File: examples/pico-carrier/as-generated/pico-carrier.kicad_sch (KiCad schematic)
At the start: 9 parts, among them J1 5V IN, J3 GP0-GP15, J4 GP16-GP28, PWR, U1 Pico

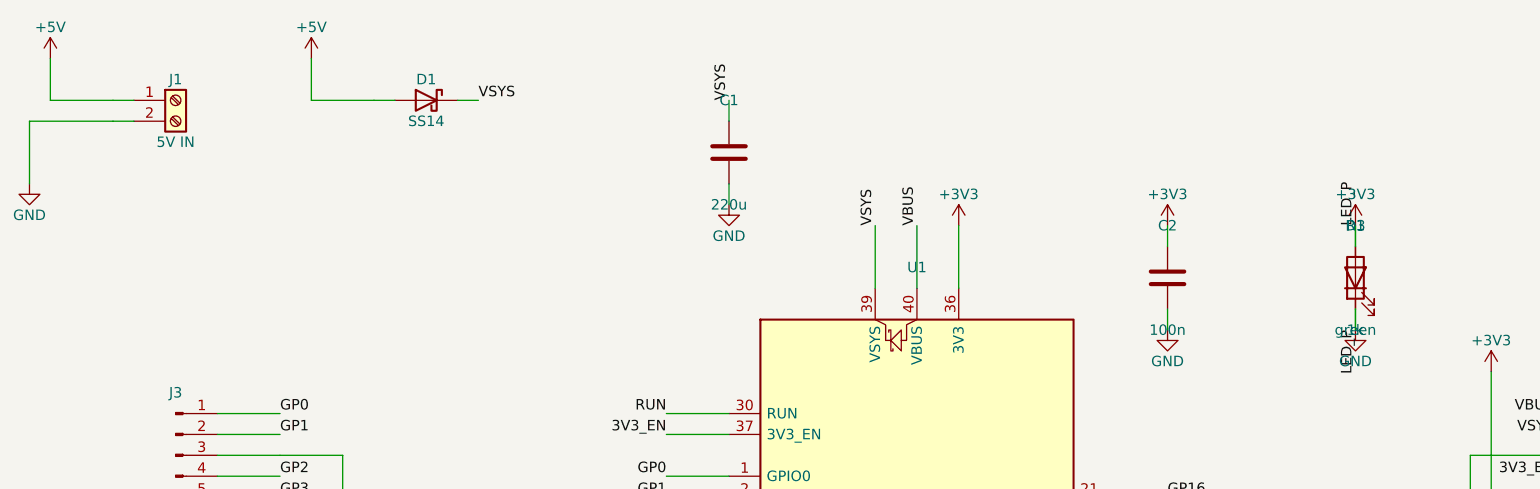
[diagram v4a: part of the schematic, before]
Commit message: Regenerate the four the text and width work changed
Designators and values off the rails they were printed on, power-named
nets at the width their rule asks for, and the buck's feedback ending
on the capacitor pad it senses at.

Co-Authored-By: Claude Fable 5 <noreply@anthropic.com>
Claude-Session: https://claude.ai/code/session_01DUj7Ltu92tWg159mCSacwY
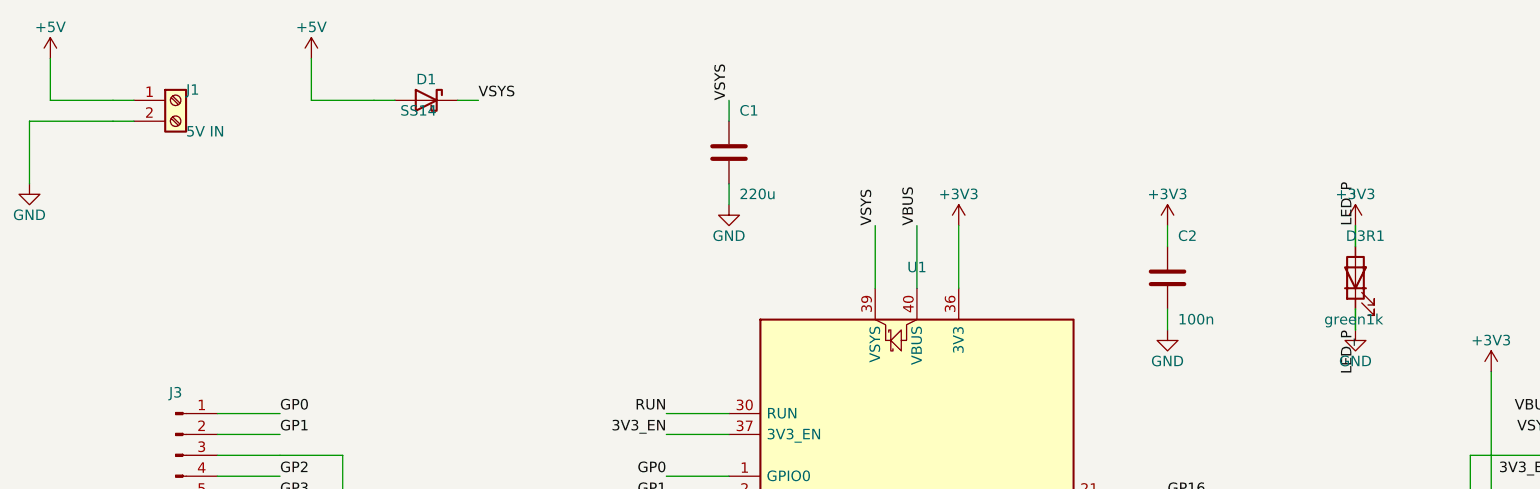
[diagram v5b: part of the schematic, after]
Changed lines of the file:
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@@
   (symbol (lib_id "Connector:Screw_Terminal_01x02") (at 60.0 39.18 0.0) (unit 1)
     (exclude_from_sim no) (in_bom yes) (on_board yes) (dnp no)
-    (property "Reference" "J1" (at 60.0 36.64 0) (effects (font (size 1.27 1.27))))
-    (property "Value" "5V IN" (at 60.0 44.26 0) (effects (font (size 1.27 1.27))))
+    (property "Reference" "J1" (at 61.27 37.91 0) (effects (font (size 1.27 1.27)) (justify left)))
+    (property "Value" "5V IN" (at 61.27 42.99 0) (effects (font (size 1.27 1.27)) (justify left)))
     (property "Footprint" "TerminalBlock_Phoenix:TerminalBlock_Phoenix_MKDS-1,5-2_1x02_P5.00mm_Horizontal" (at 60.0 39.18 0) (effects (font (size 1.27 1.27)) hide))
     (property "Datasheet" "https://www.phoenixcontact.com/product/1729128" (at 60.0 39.18 0) (effects (font (size 1.27 1.27)) hide))
@@
     (exclude_from_sim no) (in_bom yes) (on_board yes) (dnp no)
     (property "Reference" "D1" (at 90.48 36.64 0) (effects (font (size 1.27 1.27))))
-    (property "Value" "SS14" (at 90.48 41.72 0) (effects (font (size 1.27 1.27))))
+    (property "Value" "SS14" (at 91.75 40.45 0) (effects (font (size 1.27 1.27)) (justify left)))
     (property "Footprint" "Diode_SMD:D_SMA" (at 90.48 39.18 0) (effects (font (size 1.27 1.27)) hide))
     (property "Datasheet" "https://www.vishay.com/docs/88746/ss12.pdf" (at 90.48 39.18 0) (effects (font (size 1.27 1.27)) hide))
@@
   (symbol (lib_id "Device:C") (at 127.31 45.53 0.0) (unit 1)
     (exclude_from_sim no) (in_bom yes) (on_board yes) (dnp no)
-    (property "Reference" "C1" (at 127.31 39.18 0) (effects (font (size 1.27 1.27))))
-    (property "Value" "220u" (at 127.31 51.88 0) (effects (font (size 1.27 1.27))))
+    (property "Reference" "C1" (at 128.58 40.45 0) (effects (font (size 1.27 1.27)) (justify left)))
+    (property "Value" "220u" (at 128.58 50.61 0) (effects (font (size 1.27 1.27)) (justify left)))
     (property "Footprint" "Capacitor_SMD:C_1210_3225Metric" (at 127.31 45.53 0) (effects (font (size 1.27 1.27)) hide))
     (property "Datasheet" "https://product.samsungsem.com/mlcc/CL32A226KAJNNNE.do" (at 127.31 45.53 0) (effects (font (size 1.27 1.27)) hide))
@@
   (symbol (lib_id "Device:C") (at 180.65 60.77 0.0) (unit 1)
     (exclude_from_sim no) (in_bom yes) (on_board yes) (dnp no)
-    (property "Reference" "C2" (at 180.65 54.42 0) (effects (font (size 1.27 1.27))))
-    (property "Value" "100n" (at 180.65 67.12 0) (effects (font (size 1.27 1.27))))
+    (property "Reference" "C2" (at 181.92 55.69 0) (effects (font (size 1.27 1.27)) (justify left)))
+    (property "Value" "100n" (at 181.92 65.85 0) (effects (font (size 1.27 1.27)) (justify left)))
     (property "Footprint" "Capacitor_SMD:C_0805_2012Metric" (at 180.65 60.77 0) (effects (font (size 1.27 1.27)) hide))
     (property "Datasheet" "https://product.samsungsem.com/mlcc/CL21B104KBCNNNC.do" (at 180.65 60.77 0) (effects (font (size 1.27 1.27)) hide))
@@
   (symbol (lib_id "Device:R") (at 203.51 60.77 0.0) (unit 1)
     (exclude_from_sim no) (in_bom yes) (on_board yes) (dnp no)
-    (property "Reference" "R1" (at 203.51 54.42 0) (effects (font (size 1.27 1.27))))
-    (property "Value" "1k" (at 203.51 67.12 0) (effects (font (size 1.27 1.27))))
+    (property "Reference" "R1" (at 204.78 55.69 0) (effects (font (size 1.27 1.27)) (justify left)))
+    (property "Value" "1k" (at 204.78 65.85 0) (effects (font (size 1.27 1.27)) (justify left)))
     (property "Footprint" "Resistor_SMD:R_0805_2012Metric" (at 203.51 60.77 0) (effects (font (size 1.27 1.27)) hide))
     (property "Datasheet" "https://www.yageo.com/upload/media/product/productsearch/datasheet/rchip/PYu-RC_Group_51_RoHS_L_12.pdf" (at 203.51 60.77 0) (effects (font (size 1.27 1.27)) hide))
@@
   (symbol (lib_id "Device:LED") (at 203.51 60.77 90.0) (unit 1)
     (exclude_from_sim no) (in_bom yes) (on_board yes) (dnp no)
-    (property "Reference" "D3" (at 203.51 54.42 90) (effects (font (size 1.27 1.27))))
-    (property "Value" "green" (at 203.51 67.12 90) (effects (font (size 1.27 1.27))))
+    (property "Reference" "D3" (at 204.78 55.69 90) (effects (font (size 1.27 1.27)) (justify left)))
+    (property "Value" "green" (at 204.78 65.85 90) (effects (font (size 1.27 1.27)) (justify left)))
     (property "Footprint" "LED_SMD:LED_0805_2012Metric" (at 203.51 60.77 0) (effects (font (size 1.27 1.27)) hide))
     (property "Datasheet" "https://optoelectronics.liteon.com/upload/download/DS-22-98-0002/LTST-C170KGKT.pdf" (at 203.51 60.77 0) (effects (font (size 1.27 1.27)) hide))
